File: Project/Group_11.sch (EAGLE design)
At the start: 28 parts, among them J1 POWER_JACKPTH_LOCK, U1 +12v

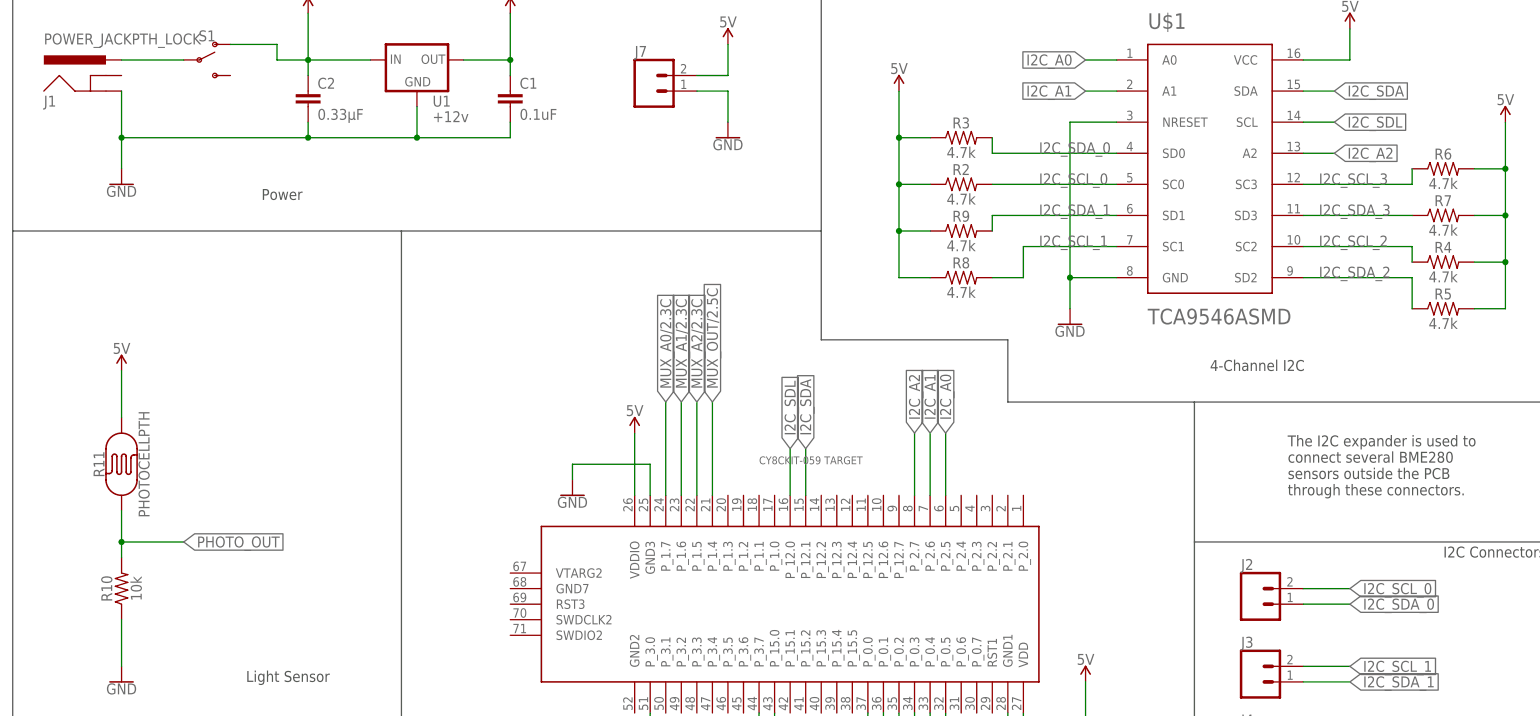
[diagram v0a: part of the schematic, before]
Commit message: Modifica Labels I2C_SCL
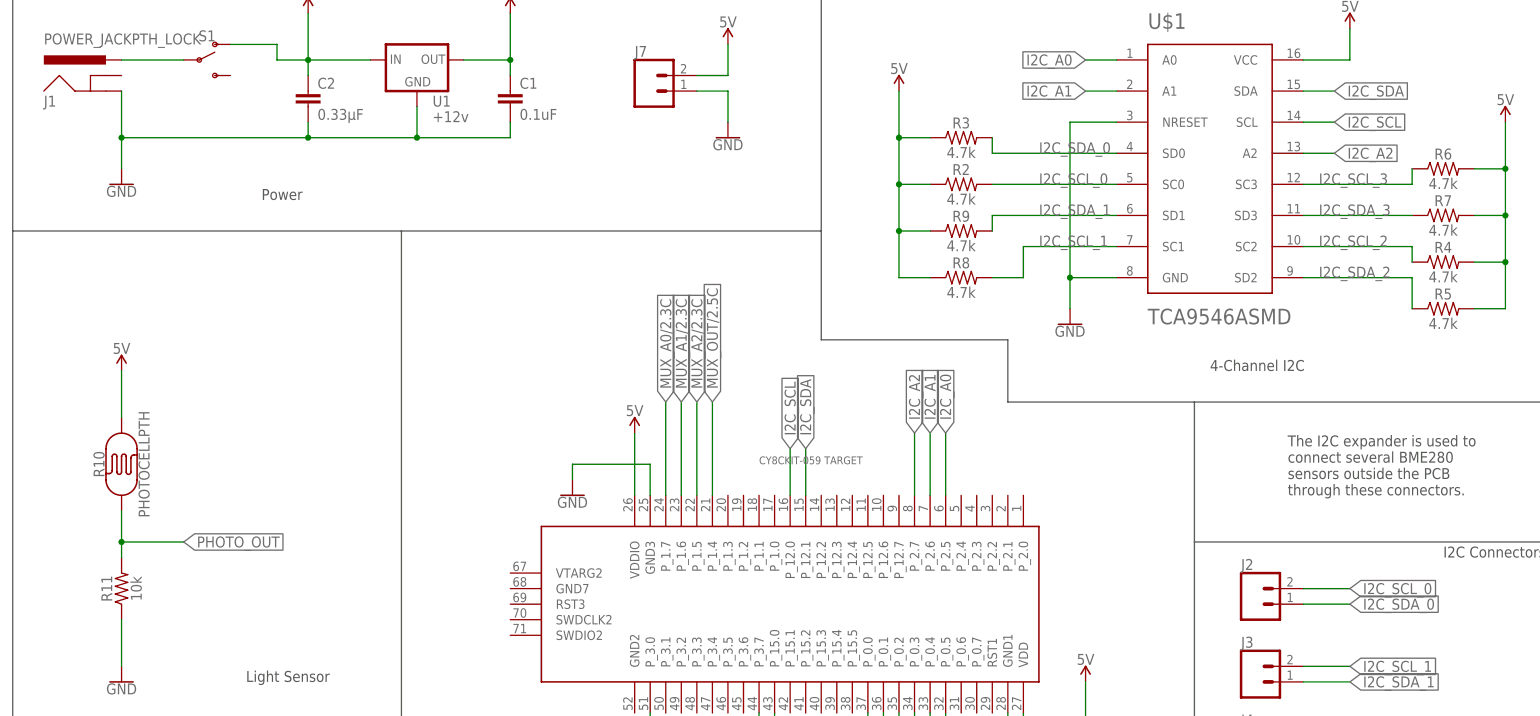
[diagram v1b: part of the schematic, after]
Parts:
- R10: value 10k -> PHOTOCELLPTH; device SparkFun-Resistors:10KOHM-0603-1/10W-1% -> SparkFun-Sensors:PHOTOCELLPTH
- R11: value PHOTOCELLPTH -> 10k; device SparkFun-Sensors:PHOTOCELLPTH -> SparkFun-Resistors:10KOHM-0603-1/10W-1%
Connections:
- net I2C_SDL renamed I2C_SCL
- net 5V: now also R10.P$2; no longer R11.P$2
- net GND: now also R11.1; no longer R10.1
- net PHOTO_OUT: now also R10.P$1, R11.2; no longer R10.2, R11.P$1
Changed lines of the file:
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@@
 <part name="U1" library="SparkFun-IC-Power" deviceset="V_REG_78XX" device="7812" value="+12v"/>
 <part name="J2" library="SparkFun-Connectors" deviceset="CONN_02" device=""/>
-<part name="R11" library="SparkFun-Sensors" deviceset="PHOTOCELL" device="PTH"/>
+<part name="R10" library="SparkFun-Sensors" deviceset="PHOTOCELL" device="PTH"/>
 <part name="U2" library="SparkFun-Sensors" deviceset="TMP36" device="GT9"/>
 <part name="D1" library="SparkFun-LED" deviceset="LED-BLUE" device="1206" value="BLUE"/>
@@
 <part name="SUPPLY9" library="SparkFun-PowerSymbols" deviceset="5V" device=""/>
 <part name="SUPPLY10" library="SparkFun-PowerSymbols" deviceset="5V" device=""/>
-<part name="R10" library="SparkFun-Resistors" deviceset="10KOHM" device="-0603-1/10W-1%" value="10k"/>
+<part name="R11" library="SparkFun-Resistors" deviceset="10KOHM" device="-0603-1/10W-1%" value="10k"/>
 <part name="SUPPLY11" library="SparkFun-PowerSymbols" deviceset="5V" device=""/>
 <part name="GND8" library="SparkFun-PowerSymbols" deviceset="GND" device=""/>
@@
 <attribute name="NAME" x="215.9" y="76.708" size="1.778" layer="95" font="vector"/>
 </instance>
-<instance part="R11" gate="G$1" x="33.02" y="93.98" smashed="yes" rot="R90">
+<instance part="R10" gate="G$1" x="33.02" y="93.98" smashed="yes" rot="R90">
 <attribute name="NAME" x="30.226" y="93.98" size="1.778" layer="95" font="vector" rot="R90" align="bottom-center"/>
 <attribute name="VALUE" x="35.814" y="93.98" size="1.778" layer="96" font="vector" rot="R90" align="top-center"/>
@@
 <attribute name="VALUE" x="259.08" y="152.654" size="1.778" layer="96" align="bottom-center"/>
 </instance>
-<instance part="R10" gate="G$1" x="33.02" y="73.66" smashed="yes" rot="R90">
+<instance part="R11" gate="G$1" x="33.02" y="73.66" smashed="yes" rot="R90">
 <attribute name="NAME" x="31.496" y="73.66" size="1.778" layer="95" font="vector" rot="R90" align="bottom-center"/>
 <attribute name="VALUE" x="34.544" y="73.66" size="1.778" layer="96" font="vector" rot="R90" align="top-center"/>
@@
 <segment>
 <pinref part="GND8" gate="1" pin="GND"/>
-<pinref part="R10" gate="G$1" pin="1"/>
+<pinref part="R11" gate="G$1" pin="1"/>
 <wire x1="33.02" y1="60.96" x2="33.02" y2="68.58" width="0.1524" layer="91"/>
 </segment>
@@
 </segment>
 <segment>
-<pinref part="R11" gate="G$1" pin="P$2"/>
+<pinref part="R10" gate="G$1" pin="P$2"/>
 <pinref part="SUPPLY11" gate="G$1" pin="5V"/>
 <wire x1="33.02" y1="101.6" x2="33.02" y2="109.22" width="0.1524" layer="91"/>
@@
 <net name="PHOTO_OUT" class="0">
 <segment>
-<pinref part="R10" gate="G$1" pin="2"/>
-<pinref part="R11" gate="G$1" pin="P$1"/>
+<pinref part="R11" gate="G$1" pin="2"/>
+<pinref part="R10" gate="G$1" pin="P$1"/>
 <wire x1="33.02" y1="78.74" x2="33.02" y2="81.28" width="0.1524" layer="91"/>
 <wire x1="33.02" y1="81.28" x2="33.02" y2="86.36" width="0.1524" layer="91"/>
@@
 <wire x1="129.54" y1="88.9" x2="129.54" y2="104.14" width="0.1524" layer="91"/>
 <label x="129.54" y="104.14" size="1.778" layer="95" rot="R90" xref="yes"/>
-</segment>
-</net>
-<net name="I2C_SDL" class="0">
-<segment>
-<pinref part="U$2" gate="G$1" pin="P_12.0"/>
-<wire x1="142.24" y1="88.9" x2="142.24" y2="96.52" width="0.1524" layer="91"/>
-<label x="142.24" y="96.52" size="1.778" layer="95" rot="R90" xref="yes"/>
-</segment>
-<segment>
-<pinref part="U$1" gate="G$1" pin="SCL"/>
-<wire x1="226.06" y1="149.86" x2="231.14" y2="149.86" width="0.1524" layer="91"/>
-<label x="231.14" y="149.86" size="1.778" layer="95" xref="yes"/>
 </segment>
 </net>
@@
 </segment>
 </net>
+<net name="I2C_SCL" class="0">
+<segment>
+<pinref part="U$1" gate="G$1" pin="SCL"/>
+<wire x1="226.06" y1="149.86" x2="231.14" y2="149.86" width="0.1524" layer="91"/>
+<label x="231.14" y="149.86" size="1.778" layer="95" xref="yes"/>
+</segment>
+<segment>
+<pinref part="U$2" gate="G$1" pin="P_12.0"/>
+<wire x1="142.24" y1="88.9" x2="142.24" y2="96.52" width="0.1524" layer="91"/>
+<label x="142.24" y="96.52" size="1.778" layer="95" rot="R90" xref="yes"/>
+</segment>
+</net>

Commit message: Modifica di libreria e schematico su dev
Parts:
- added U$3: TMUX1208SMD, Group_11_Library:TMUX1208SMD
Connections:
- new net MUX_A0/1.3C: U$3.A0
- new net MUX_A1/1.4C: U$3.A1
- new net MUX_A2/1.4C: U$3.A2
- new net MUX_OUT/1.4C: U$3.D
- new net N$1: J8.8, U$3.S1
- new net N$10: J8.7, U$3.S2
- new net N$11: J8.6, U$3.S3
- new net N$12: J8.5, U$3.S4
- new net N$13: J8.4, U$3.S5
- new net N$14: J8.3, U$3.S6
- new net N$15: J8.2, U$3.S7
- new net N$16: J8.1, U$3.S8
- net 5V: now also C3.1, U$3.E.N., U$3.VDD
- net GND: now also C3.2, U$3.GND
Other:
- moved on the sheet: C3, J8
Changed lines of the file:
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@@
 <part name="GND9" library="SparkFun-PowerSymbols" deviceset="GND" device=""/>
 <part name="SUPPLY12" library="SparkFun-PowerSymbols" deviceset="5V" device=""/>
+<part name="U$3" library="Group_11_Library" deviceset="TMUX1208" device="SMD"/>
 </parts>
 <sheets>
@@
 <attribute name="NAME" x="116.84" y="160.528" size="1.778" layer="95" font="vector"/>
 </instance>
-<instance part="J8" gate="G$1" x="396.24" y="104.14" smashed="yes">
-<attribute name="VALUE" x="391.16" y="91.694" size="1.778" layer="96" font="vector"/>
-<attribute name="NAME" x="391.16" y="117.348" size="1.778" layer="95" font="vector"/>
+<instance part="J8" gate="G$1" x="383.54" y="96.52" smashed="yes">
+<attribute name="VALUE" x="378.46" y="84.074" size="1.778" layer="96" font="vector"/>
+<attribute name="NAME" x="378.46" y="109.728" size="1.778" layer="95" font="vector"/>
 </instance>
 <instance part="J6" gate="G$1" x="162.56" y="40.64" smashed="yes" rot="R90">
@@
 <attribute name="DESIGNER" x="518.36" y="6.35" size="2.54" layer="94" font="vector"/>
 </instance>
-<instance part="C3" gate="G$1" x="464.82" y="101.6" smashed="yes">
-<attribute name="NAME" x="466.344" y="104.521" size="1.778" layer="95" font="vector"/>
-<attribute name="VALUE" x="466.344" y="99.441" size="1.778" layer="96" font="vector"/>
-</instance>
-<instance part="SUPPLY1" gate="G$1" x="444.5" y="134.62" smashed="yes">
-<attribute name="VALUE" x="444.5" y="137.414" size="1.778" layer="96" align="bottom-center"/>
-</instance>
-<instance part="SUPPLY2" gate="G$1" x="441.96" y="88.9" smashed="yes">
-<attribute name="VALUE" x="441.96" y="91.694" size="1.778" layer="96" align="bottom-center"/>
-</instance>
-<instance part="GND1" gate="1" x="436.88" y="63.5" smashed="yes">
-<attribute name="VALUE" x="436.88" y="63.246" size="1.778" layer="96" align="top-center"/>
+<instance part="C3" gate="G$1" x="485.14" y="91.44" smashed="yes">
+<attribute name="NAME" x="486.664" y="94.361" size="1.778" layer="95" font="vector"/>
+<attribute name="VALUE" x="486.664" y="89.281" size="1.778" layer="96" font="vector"/>
+</instance>
+<instance part="SUPPLY1" gate="G$1" x="449.58" y="111.76" smashed="yes">
+<attribute name="VALUE" x="449.58" y="114.554" size="1.778" layer="96" align="bottom-center"/>
+</instance>
+<instance part="SUPPLY2" gate="G$1" x="474.98" y="81.28" smashed="yes">
+<attribute name="VALUE" x="474.98" y="84.074" size="1.778" layer="96" align="bottom-center"/>
+</instance>
+<instance part="GND1" gate="1" x="449.58" y="63.5" smashed="yes">
+<attribute name="VALUE" x="449.58" y="63.246" size="1.778" layer="96" align="top-center"/>
 </instance>
 <instance part="GND2" gate="1" x="101.6" y="17.78" smashed="yes">
@@
 <instance part="SUPPLY12" gate="G$1" x="33.02" y="38.1" smashed="yes">
 <attribute name="VALUE" x="33.02" y="40.894" size="1.778" layer="96" align="bottom-center"/>
+</instance>
+<instance part="U$3" gate="G$1" x="426.72" y="88.9" smashed="yes">
+<attribute name="NAME" x="419.1" y="111.76" size="2.54" layer="95"/>
+<attribute name="VALUE" x="414.02" y="63.5" size="2.54" layer="96"/>
 </instance>
 </instances>
@@
 <segment>
 <pinref part="J6" gate="G$1" pin="1"/>
-<pinref part="U$2" gate="G$1" pin="P_12.1"/>
 <pinref part="U$2" gate="G$1" pin="P_0.5"/>
 <wire x1="167.64" y1="45.72" x2="167.64" y2="53.34" width="0.1524" layer="91"/>
-<wire x1="144.78" y1="88.9" x2="144.78" y2="96.52" width="0.1524" layer="91"/>
-<label x="144.78" y="96.52" size="1.778" layer="95" rot="R90" xref="yes"/>
 </segment>
 <segment>
@@
 <wire x1="226.06" y1="154.94" x2="231.14" y2="154.94" width="0.1524" layer="91"/>
 <label x="231.14" y="154.94" size="1.778" layer="95" xref="yes"/>
+</segment>
+<segment>
+<pinref part="U$2" gate="G$1" pin="P_12.1"/>
+<wire x1="144.78" y1="88.9" x2="144.78" y2="96.52" width="0.1524" layer="91"/>
+<label x="144.78" y="96.52" size="1.778" layer="95" rot="R90" xref="yes"/>
 </segment>
 </net>
@@
 <wire x1="33.02" y1="22.86" x2="33.02" y2="15.24" width="0.1524" layer="91"/>
 </segment>
+<segment>
+<pinref part="U$3" gate="G$1" pin="GND"/>
+<wire x1="439.42" y1="71.12" x2="449.58" y2="71.12" width="0.1524" layer="91"/>
+<pinref part="C3" gate="G$1" pin="2"/>
+<wire x1="449.58" y1="71.12" x2="485.14" y2="71.12" width="0.1524" layer="91"/>
+<wire x1="485.14" y1="71.12" x2="485.14" y2="88.9" width="0.1524" layer="91"/>
+<pinref part="GND1" gate="1" pin="GND"/>
+<wire x1="449.58" y1="71.12" x2="449.58" y2="66.04" width="0.1524" layer="91"/>
+<junction x="449.58" y="71.12"/>
+</segment>
 </net>
 <net name="N$2" class="0">
@@
 <wire x1="33.02" y1="27.94" x2="33.02" y2="38.1" width="0.1524" layer="91"/>
 </segment>
+<segment>
+<pinref part="C3" gate="G$1" pin="1"/>
+<pinref part="U$3" gate="G$1" pin="VDD"/>
+<wire x1="485.14" y1="96.52" x2="485.14" y2="106.68" width="0.1524" layer="91"/>
+<wire x1="485.14" y1="106.68" x2="449.58" y2="106.68" width="0.1524" layer="91"/>
+<pinref part="SUPPLY1" gate="G$1" pin="5V"/>
+<wire x1="449.58" y1="106.68" x2="439.42" y2="106.68" width="0.1524" layer="91"/>
+<wire x1="449.58" y1="111.76" x2="449.58" y2="106.68" width="0.1524" layer="91"/>
+<junction x="449.58" y="106.68"/>
+</segment>
+<segment>
+<pinref part="U$3" gate="G$1" pin="E.N."/>
+<wire x1="439.42" y1="76.2" x2="474.98" y2="76.2" width="0.1524" layer="91"/>
+<pinref part="SUPPLY2" gate="G$1" pin="5V"/>
+<wire x1="474.98" y1="76.2" x2="474.98" y2="81.28" width="0.1524" layer="91"/>
+</segment>
 </net>
 <net name="N$9" class="0">
@@
 </segment>
 </net>
+<net name="N$1" class="0">
+<segment>
+<pinref part="J8" gate="G$1" pin="8"/>
+<pinref part="U$3" gate="G$1" pin="S1"/>
+<wire x1="388.62" y1="106.68" x2="414.02" y2="106.68" width="0.1524" layer="91"/>
+</segment>
+</net>
+<net name="N$10" class="0">
+<segment>
+<pinref part="J8" gate="G$1" pin="7"/>
+<wire x1="388.62" y1="104.14" x2="411.48" y2="104.14" width="0.1524" layer="91"/>
+<wire x1="411.48" y1="104.14" x2="411.48" y2="101.6" width="0.1524" layer="91"/>
+<pinref part="U$3" gate="G$1" pin="S2"/>
+<wire x1="411.48" y1="101.6" x2="414.02" y2="101.6" width="0.1524" layer="91"/>
+</segment>
+</net>
+<net name="N$11" class="0">
+<segment>
+<pinref part="J8" gate="G$1" pin="6"/>
+<wire x1="388.62" y1="101.6" x2="408.94" y2="101.6" width="0.1524" layer="91"/>
+<wire x1="408.94" y1="101.6" x2="408.94" y2="96.52" width="0.1524" layer="91"/>
+<pinref part="U$3" gate="G$1" pin="S3"/>
+<wire x1="408.94" y1="96.52" x2="414.02" y2="96.52" width="0.1524" layer="91"/>
+</segment>
+</net>
+<net name="N$12" class="0">
+<segment>
+<pinref part="J8" gate="G$1" pin="5"/>
+<wire x1="388.62" y1="99.06" x2="406.4" y2="99.06" width="0.1524" layer="91"/>
+<wire x1="406.4" y1="99.06" x2="406.4" y2="91.44" width="0.1524" layer="91"/>
+<pinref part="U$3" gate="G$1" pin="S4"/>
+<wire x1="406.4" y1="91.44" x2="414.02" y2="91.44" width="0.1524" layer="91"/>
+</segment>
+</net>
+<net name="N$13" class="0">
+<segment>
+<pinref part="J8" gate="G$1" pin="4"/>
+<wire x1="388.62" y1="96.52" x2="403.86" y2="96.52" width="0.1524" layer="91"/>
+<wire x1="403.86" y1="96.52" x2="403.86" y2="86.36" width="0.1524" layer="91"/>
+<pinref part="U$3" gate="G$1" pin="S5"/>
+<wire x1="403.86" y1="86.36" x2="414.02" y2="86.36" width="0.1524" layer="91"/>
+</segment>
+</net>
+<net name="N$14" class="0">
+<segment>
+<pinref part="J8" gate="G$1" pin="3"/>
+<wire x1="388.62" y1="93.98" x2="401.32" y2="93.98" width="0.1524" layer="91"/>
+<wire x1="401.32" y1="93.98" x2="401.32" y2="81.28" width="0.1524" layer="91"/>
+<pinref part="U$3" gate="G$1" pin="S6"/>
+<wire x1="401.32" y1="81.28" x2="414.02" y2="81.28" width="0.1524" layer="91"/>
+</segment>
+</net>
+<net name="N$15" class="0">
+<segment>
+<pinref part="J8" gate="G$1" pin="2"/>
+<wire x1="388.62" y1="91.44" x2="398.78" y2="91.44" width="0.1524" layer="91"/>
+<wire x1="398.78" y1="91.44" x2="398.78" y2="76.2" width="0.1524" layer="91"/>
+<pinref part="U$3" gate="G$1" pin="S7"/>
+<wire x1="398.78" y1="76.2" x2="414.02" y2="76.2" width="0.1524" layer="91"/>
+</segment>
+</net>
+<net name="N$16" class="0">
+<segment>
+<pinref part="J8" gate="G$1" pin="1"/>
+<wire x1="388.62" y1="88.9" x2="396.24" y2="88.9" width="0.1524" layer="91"/>
+<wire x1="396.24" y1="88.9" x2="396.24" y2="71.12" width="0.1524" layer="91"/>
+<pinref part="U$3" gate="G$1" pin="S8"/>
+<wire x1="396.24" y1="71.12" x2="414.02" y2="71.12" width="0.1524" layer="91"/>
+</segment>
+</net>
+<net name="MUX_A0/1.3C" class="0">
+<segment>
+<pinref part="U$3" gate="G$1" pin="A0"/>
+<wire x1="439.42" y1="96.52" x2="444.5" y2="96.52" width="0.1524" layer="91"/>
+<label x="444.5" y="96.52" size="1.778" layer="95" xref="yes"/>
+</segment>
+</net>
+<net name="MUX_A1/1.4C" class="0">
+<segment>
+<pinref part="U$3" gate="G$1" pin="A1"/>
+<wire x1="439.42" y1="91.44" x2="444.5" y2="91.44" width="0.1524" layer="91"/>
+<label x="444.5" y="91.44" size="1.778" layer="95" xref="yes"/>
+</segment>
+</net>
+<net name="MUX_A2/1.4C" class="0">
+<segment>
+<pinref part="U$3" gate="G$1" pin="A2"/>
+<wire x1="439.42" y1="86.36" x2="444.5" y2="86.36" width="0.1524" layer="91"/>
+<label x="444.5" y="86.36" size="1.778" layer="95" xref="yes"/>
+</segment>
+</net>
+<net name="MUX_OUT/1.4C" class="0">
+<segment>
+<pinref part="U$3" gate="G$1" pin="D"/>
+<wire x1="439.42" y1="81.28" x2="444.5" y2="81.28" width="0.1524" layer="91"/>
+<label x="444.5" y="81.28" size="1.778" layer="95" xref="yes"/>
+</segment>
+</net>

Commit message: Modifica symbols e schematico aggiornato
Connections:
- new net N$17: J6.1, U$2.P_0.5
- new net N$18: C3.2, U$3.GND
- net 5V: now also R2.2, R3.2, R8.2, R9.2; no longer R2.1, R3.1, R8.1, R9.1
- net GND: no longer C3.2, U$3.GND
- net I2C_SCL_0: now also R2.1; no longer R2.2
- net I2C_SCL_1: now also R8.1; no longer R8.2
- net I2C_SDA: no longer J6.1, U$2.P_0.5
- net I2C_SDA_0: now also R3.1; no longer R3.2
- net I2C_SDA_1: now also R9.1; no longer R9.2
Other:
- moved on the sheet: D1, J6, J8, R1, R2, R3, R4, R5, R6, R7, R8, R9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

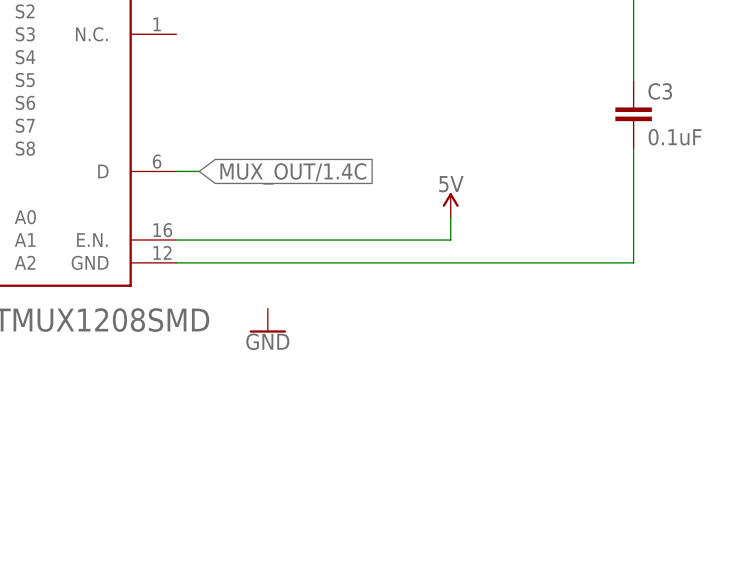
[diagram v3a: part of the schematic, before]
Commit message: Aggiunta GND
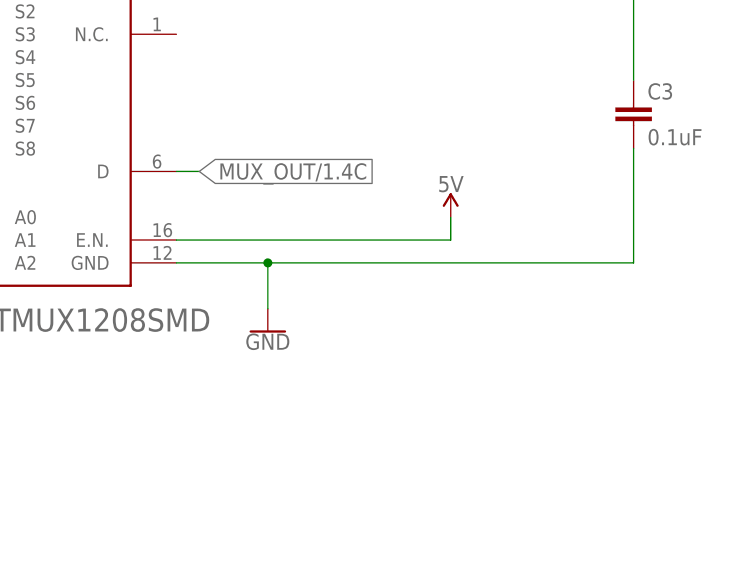
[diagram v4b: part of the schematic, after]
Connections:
- removed net N$18: C3.2, U$3.GND
- net GND: now also C3.2, U$3.GND
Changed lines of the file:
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@@
 <pinref part="GND7" gate="1" pin="GND"/>
+</segment>
+<segment>
+<pinref part="C3" gate="G$1" pin="2"/>
+<wire x1="434.34" y1="76.2" x2="444.5" y2="76.2" width="0.1524" layer="91"/>
+<wire x1="444.5" y1="76.2" x2="485.14" y2="76.2" width="0.1524" layer="91"/>
+<wire x1="485.14" y1="76.2" x2="485.14" y2="88.9" width="0.1524" layer="91"/>
+<pinref part="U$3" gate="G$1" pin="GND"/>
+<pinref part="GND1" gate="1" pin="GND"/>
+<wire x1="444.5" y1="76.2" x2="444.5" y2="71.12" width="0.1524" layer="91"/>
+<junction x="444.5" y="76.2"/>
 </segment>
 </net>
@@
 </segment>
 </net>
-<net name="N$18" class="0">
-<segment>
-<pinref part="C3" gate="G$1" pin="2"/>
-<wire x1="434.34" y1="76.2" x2="485.14" y2="76.2" width="0.1524" layer="91"/>
-<wire x1="485.14" y1="76.2" x2="485.14" y2="88.9" width="0.1524" layer="91"/>
-<pinref part="U$3" gate="G$1" pin="GND"/>
-</segment>
-</net>
